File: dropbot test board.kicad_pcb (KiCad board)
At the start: 2 copper layers, 50.2 x 23.5 mm, 43 parts, among them J1 CONN_40, P1 CONN_1

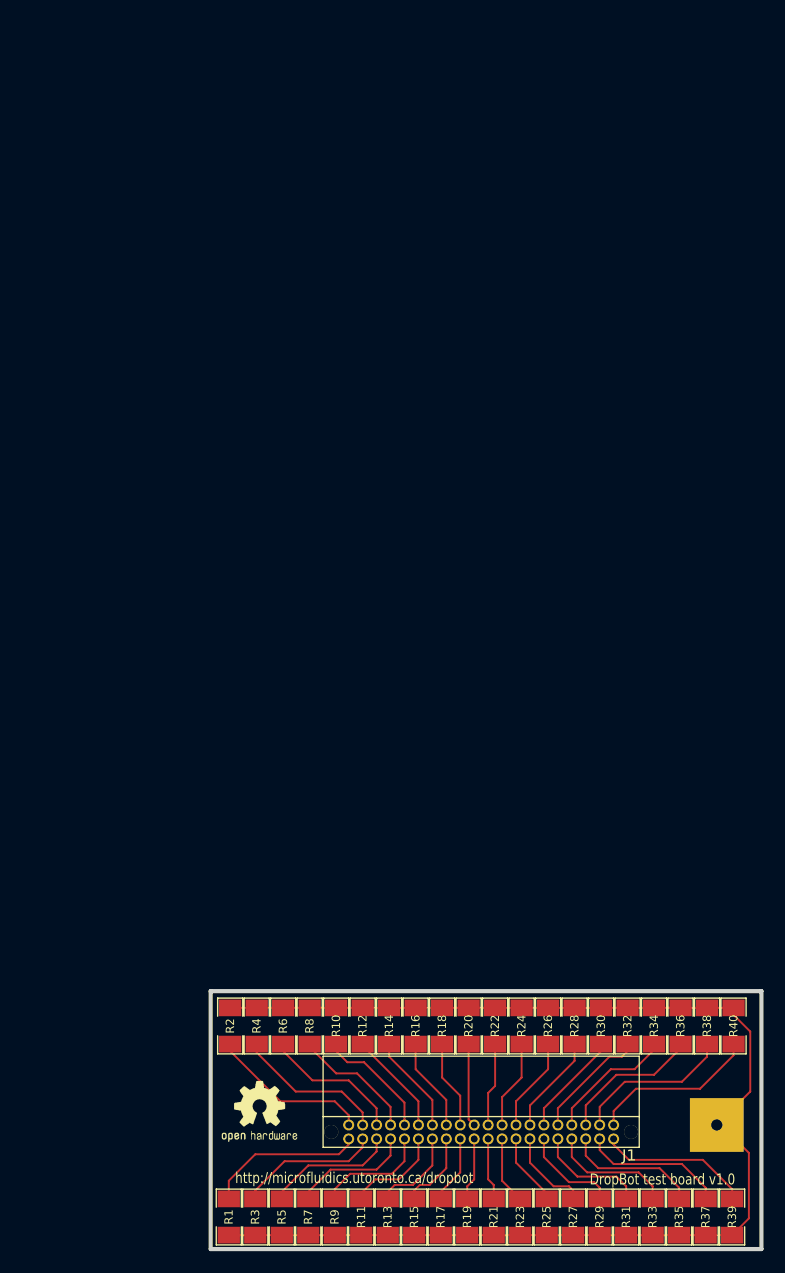
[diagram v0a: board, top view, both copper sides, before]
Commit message: Resize pages to 8.5x11" and set metadata
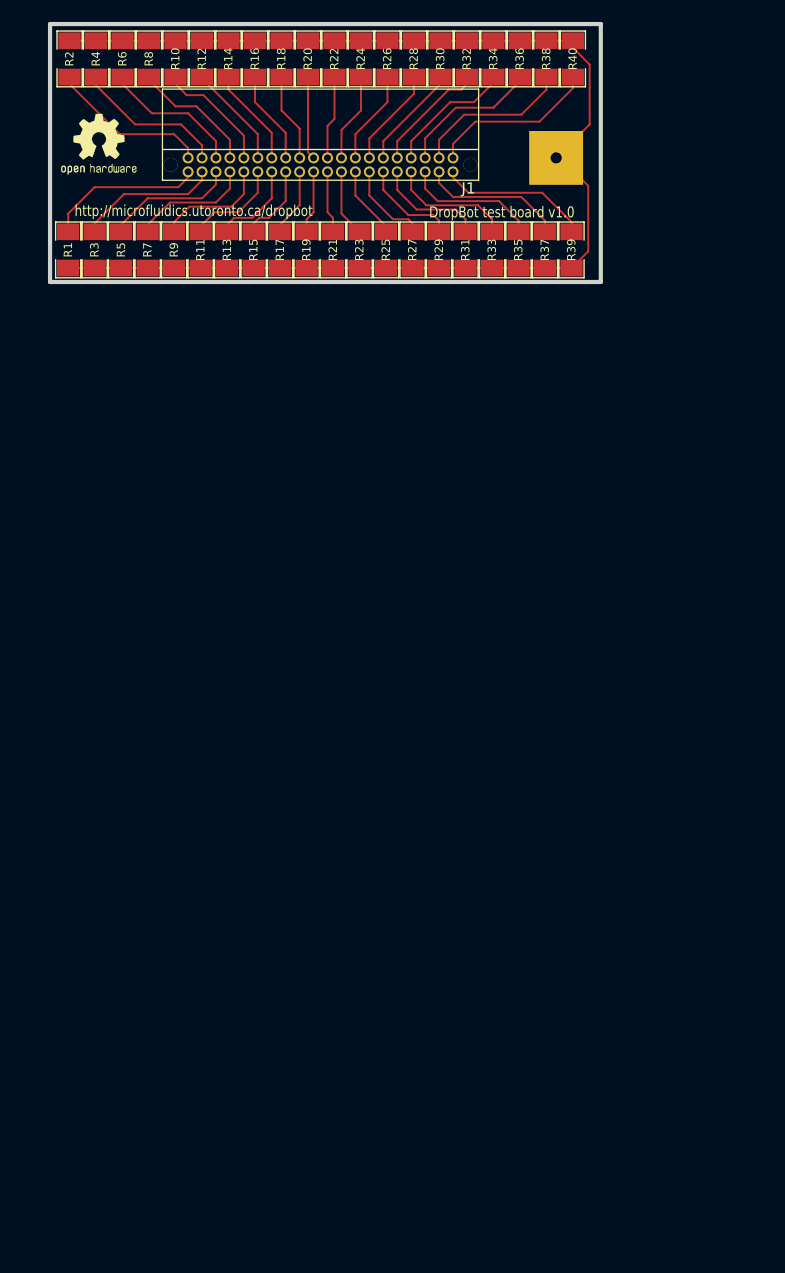
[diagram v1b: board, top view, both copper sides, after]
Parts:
- moved P1 89.3 mm to (65.1, 31.4)
- moved G*** 89.3 mm to (19.7, 26.5)
- moved J1 89.3 mm to (43.7, 32.1)
- moved R1 89.3 mm to (20.7, 39.8)
- moved R10 89.3 mm to (30.5, 22.4)
- moved R11 89.3 mm to (32.7, 39.8)
- moved R12 89.3 mm to (32.9, 22.4)
- moved R13 89.3 mm to (35.2, 39.8)
- moved R14 89.3 mm to (35.3, 22.4)
- moved R15 89.3 mm to (37.6, 39.8)
- moved R16 89.3 mm to (37.7, 22.4)
- moved R17 89.3 mm to (40.0, 39.8)
- moved R18 89.3 mm to (40.1, 22.4)
- moved R19 89.3 mm to (42.4, 39.8)
- moved R2 89.3 mm to (20.8, 22.4)
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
